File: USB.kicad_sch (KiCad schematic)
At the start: 41 parts, among them CON1 MicroSD_socket, J4 24FLZ-SM2-TB, Q1 AO3401A, U3 FDS9926A

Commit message: All key features are in the schematic.
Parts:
- added J3: PDM MEMS Mic, symbol Connector_Generic:Conn_01x05
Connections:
- net +3.3V: now also J3.1 (Pin_1)
- net GND: now also J3.2 (Pin_2), J3.3 (Pin_3)
- new net DMIC_CLK: J3.4 (Pin_4)
- new net DMIC_DATA: J3.5 (Pin_5)

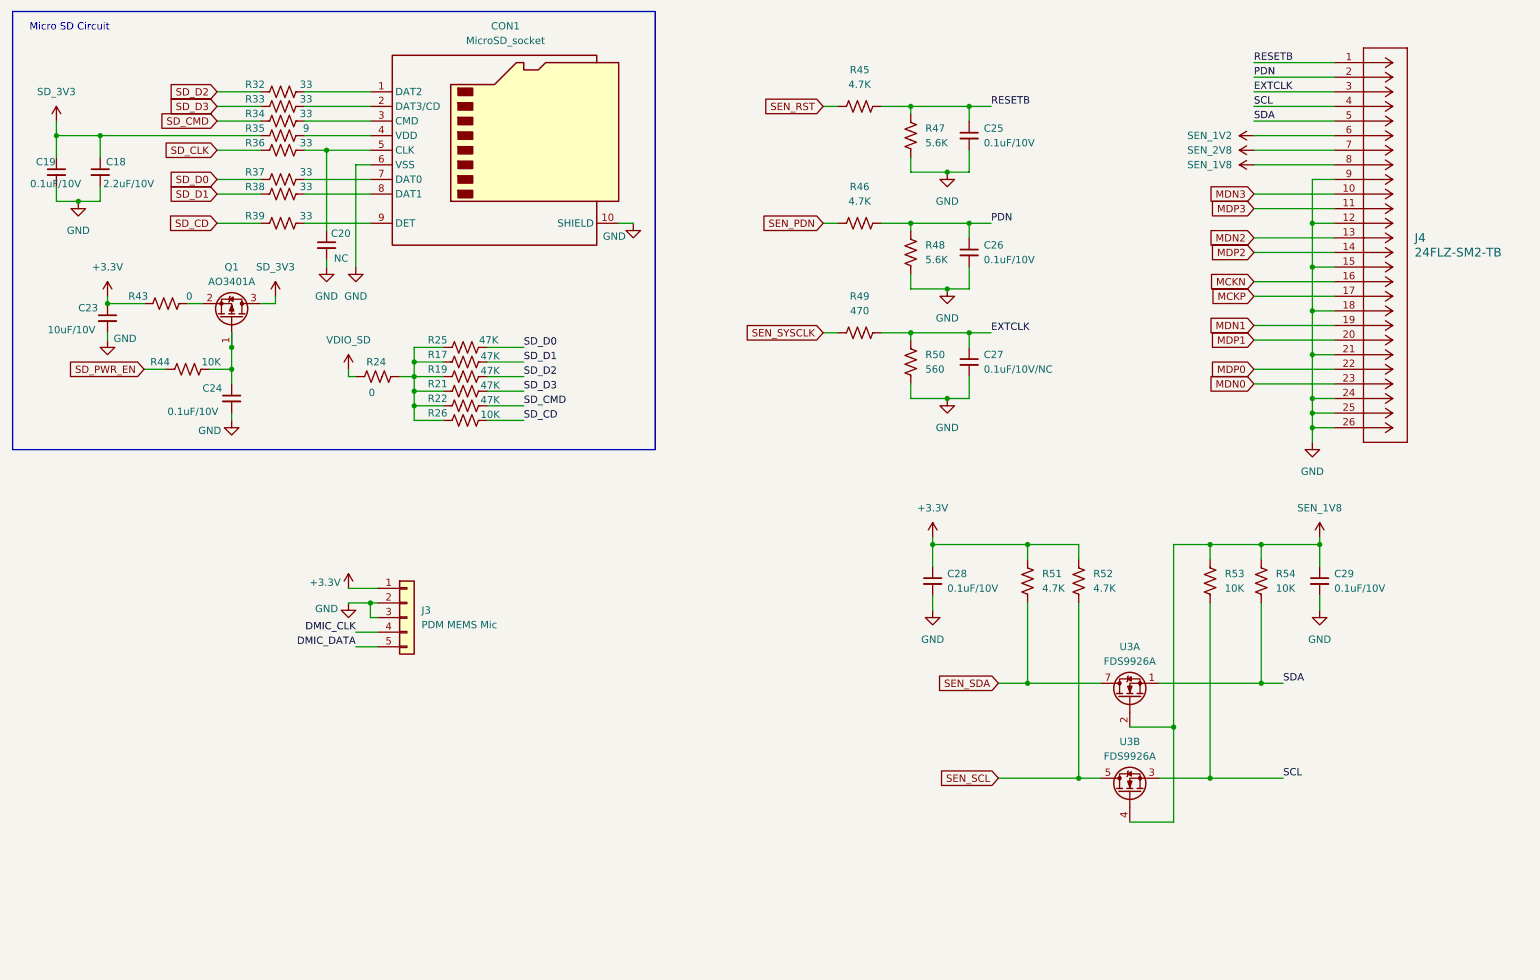
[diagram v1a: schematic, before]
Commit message: All footprints configured correctly. Next step is layout
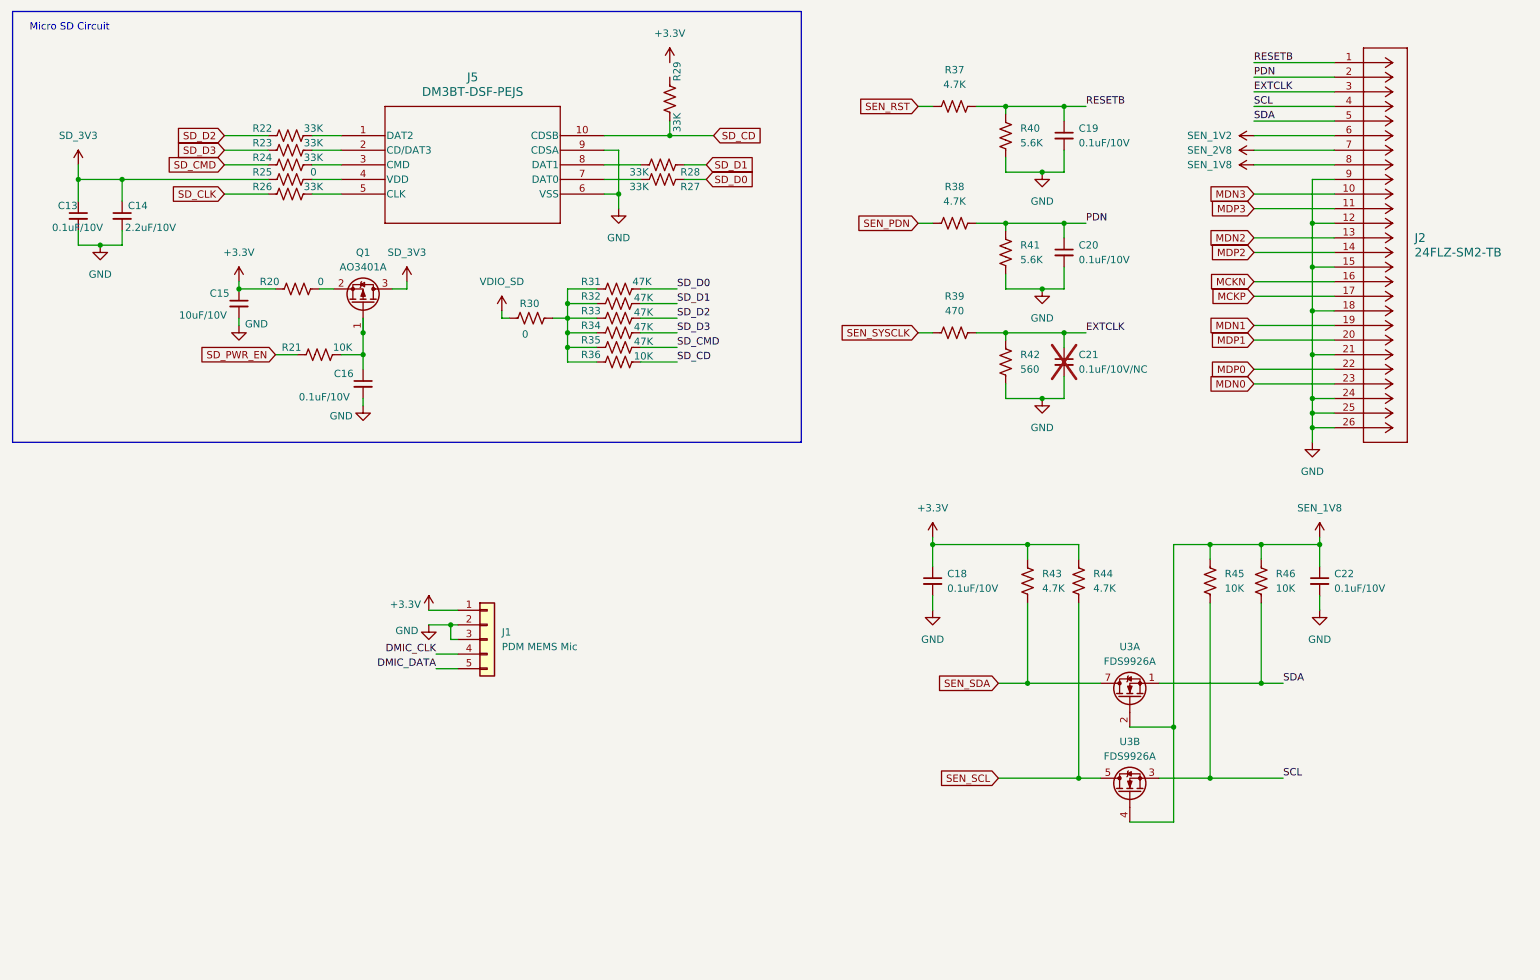
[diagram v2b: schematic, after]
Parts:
- removed C20: NC, symbol Device:C_Small
- removed CON1: MicroSD_socket, symbol Connector:Micro_SD_Card_Det1
- added J5: DM3BT-DSF-PEJS, DM3BT-DSF-PEJS_HIR, symbol 2026-01-21_09-53-59:DM3BT-DSF-PEJS
- C13: renamed from C19; footprint (none) -> Capacitor_SMD:C_0201_0603Metric_Pad0.64x0.40mm_HandSolder
- C14: renamed from C18; footprint (none) -> Capacitor_SMD:C_0201_0603Metric_Pad0.64x0.40mm_HandSolder
- C15: renamed from C23; footprint (none) -> Capacitor_SMD:C_0201_0603Metric_Pad0.64x0.40mm_HandSolder
- C16: renamed from C24; footprint (none) -> Capacitor_SMD:C_0201_0603Metric_Pad0.64x0.40mm_HandSolder
- C18: renamed from C28; footprint (none) -> Capacitor_SMD:C_0201_0603Metric_Pad0.64x0.40mm_HandSolder
- C19: renamed from C25; footprint (none) -> Capacitor_SMD:C_0201_0603Metric_Pad0.64x0.40mm_HandSolder
- C20: renamed from C26; footprint (none) -> Capacitor_SMD:C_0201_0603Metric_Pad0.64x0.40mm_HandSolder
- C21: renamed from C27; footprint (none) -> Capacitor_SMD:C_0201_0603Metric_Pad0.64x0.40mm_HandSolder; now not fitted
- C22: renamed from C29; footprint (none) -> Capacitor_SMD:C_0201_0603Metric_Pad0.64x0.40mm_HandSolder
- J1: renamed from J3; footprint (none) -> Adafruit:Adafruit MEMS 3492
- R20: renamed from R43; footprint (none) -> Resistor_SMD:R_0201_0603Metric_Pad0.64x0.40mm_HandSolder
- R21: renamed from R44; footprint (none) -> Resistor_SMD:R_0201_0603Metric_Pad0.64x0.40mm_HandSolder
- R22: renamed from R32; value 33 -> 33K; footprint (none) -> Resistor_SMD:R_0201_0603Metric_Pad0.64x0.40mm_HandSolder
- R23: renamed from R33; value 33 -> 33K; footprint (none) -> Resistor_SMD:R_0201_0603Metric_Pad0.64x0.40mm_HandSolder
- R24: renamed from R34; value 33 -> 33K; footprint (none) -> Resistor_SMD:R_0201_0603Metric_Pad0.64x0.40mm_HandSolder
- R25: renamed from R35; value 9 -> 0; footprint (none) -> Resistor_SMD:R_0201_0603Metric_Pad0.64x0.40mm_HandSolder
- R26: renamed from R36; value 33 -> 33K; footprint (none) -> Resistor_SMD:R_0201_0603Metric_Pad0.64x0.40mm_HandSolder
- R27: renamed from R37; value 33 -> 33K; footprint (none) -> Resistor_SMD:R_0201_0603Metric_Pad0.64x0.40mm_HandSolder
- R28: renamed from R38; value 33 -> 33K; footprint (none) -> Resistor_SMD:R_0201_0603Metric_Pad0.64x0.40mm_HandSolder
- R29: renamed from R39; value 33 -> 33K; footprint (none) -> Resistor_SMD:R_0201_0603Metric_Pad0.64x0.40mm_HandSolder
- R30: renamed from R24; footprint (none) -> Resistor_SMD:R_0201_0603Metric_Pad0.64x0.40mm_HandSolder
- R31: renamed from R25; footprint (none) -> Resistor_SMD:R_0201_0603Metric_Pad0.64x0.40mm_HandSolder
- R32: renamed from R17; footprint (none) -> Resistor_SMD:R_0201_0603Metric_Pad0.64x0.40mm_HandSolder
- R33: renamed from R19; footprint (none) -> Resistor_SMD:R_0201_0603Metric_Pad0.64x0.40mm_HandSolder
- R34: renamed from R21; footprint (none) -> Resistor_SMD:R_0201_0603Metric_Pad0.64x0.40mm_HandSolder
- R35: renamed from R22; footprint (none) -> Resistor_SMD:R_0201_0603Metric_Pad0.64x0.40mm_HandSolder
- R36: renamed from R26; footprint (none) -> Resistor_SMD:R_0201_0603Metric_Pad0.64x0.40mm_HandSolder
- R37: renamed from R45; footprint (none) -> Resistor_SMD:R_0201_0603Metric_Pad0.64x0.40mm_HandSolder
- R38: renamed from R46; footprint (none) -> Resistor_SMD:R_0201_0603Metric_Pad0.64x0.40mm_HandSolder
- R39: renamed from R49; footprint (none) -> Resistor_SMD:R_0201_0603Metric_Pad0.64x0.40mm_HandSolder
- R40: renamed from R47; footprint (none) -> Resistor_SMD:R_0201_0603Metric_Pad0.64x0.40mm_HandSolder
- R41: renamed from R48; footprint (none) -> Resistor_SMD:R_0201_0603Metric_Pad0.64x0.40mm_HandSolder
- R42: renamed from R50; footprint (none) -> Resistor_SMD:R_0201_0603Metric_Pad0.64x0.40mm_HandSolder
- R43: renamed from R51; footprint (none) -> Resistor_SMD:R_0201_0603Metric_Pad0.64x0.40mm_HandSolder
- R44: renamed from R52; footprint (none) -> Resistor_SMD:R_0201_0603Metric_Pad0.64x0.40mm_HandSolder
- R45: renamed from R53; footprint (none) -> Resistor_SMD:R_0201_0603Metric_Pad0.64x0.40mm_HandSolder
- R46: renamed from R54; footprint (none) -> Resistor_SMD:R_0201_0603Metric_Pad0.64x0.40mm_HandSolder
- renumbered J4 to J2
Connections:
- net GND: now also J5.6 (VSS), J5.9 (CDSA)
- net SD_CD: now also R29.2, J5.10 (CDSB); no longer R29.1
- net at R24.2: now also J5.3 (CMD)
- net at R28.2: now also J5.8 (DAT1)
- net at R27.2: now also J5.7 (DAT0)
- net at R25.2: now also J5.4 (VDD)
- net at R26.2: now also J5.5 (CLK)
- net at R23.2: now also J5.2 (CD/DAT3)
- net at R22.2: now also J5.1 (DAT2)
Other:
- moved on the sheet: C13, C14, C15, C16, C19, C20, J1, Q1, R20, R21, R22, R23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

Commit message: In the middle of layout. WIP
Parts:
- removed R20, R25, R30: 0, Resistor_SMD:R_0201_0603Metric_Pad0.64x0.40mm_HandSolder, symbol Device:R_US
- added TP6: SD_3.3V_TP, TestPoint:TestPoint_Pad_D1.5mm, symbol Connector:TestPoint
- C13, C16, C18, C19, C20, C22: value 0.1uF/10V -> 0.1uF
- C14: value 2.2uF/10V -> 2.2uF
- C15: value 10uF/10V -> 10uF
- C21: value 0.1uF/10V/NC -> 0.1uF/NC
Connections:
- net +3.3V: now also Q1.2 (S), R29.1
- net SD_3V3: now also J5.4 (VDD), TP6.1
- net VDIO_SD: now also R31.1, R32.1, R33.1, R34.1, R35.1, R36.1
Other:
- moved on the sheet: C15

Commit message: Breakthrough in PCB layout. WIP
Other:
- moved on the sheet: J1
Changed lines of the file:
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@@
 	)
 	(junction
-		(at 93.98 124.46)
+		(at 120.65 120.65)
 		(diameter 0)
 		(color 0 0 0 0)
@@
 	(wire
 		(pts
-			(xy 90.17 121.92) (xy 95.25 121.92)
+			(xy 116.84 118.11) (xy 121.92 118.11)
 		)
 		(stroke
@@
 	(wire
 		(pts
-			(xy 90.17 124.46) (xy 93.98 124.46)
+			(xy 116.84 120.65) (xy 120.65 120.65)
 		)
 		(stroke
@@
 	(wire
 		(pts
-			(xy 91.44 129.54) (xy 95.25 129.54)
+			(xy 118.11 125.73) (xy 121.92 125.73)
 		)
 		(stroke
@@
 	(wire
 		(pts
-			(xy 93.98 124.46) (xy 95.25 124.46)
+			(xy 120.65 120.65) (xy 121.92 120.65)
 		)
 		(stroke
@@
 	(wire
 		(pts
-			(xy 91.44 132.08) (xy 95.25 132.08)
+			(xy 118.11 128.27) (xy 121.92 128.27)
 		)
 		(stroke
@@
 	(wire
 		(pts
-			(xy 93.98 127) (xy 93.98 124.46)
+			(xy 120.65 123.19) (xy 120.65 120.65)
 		)
 		(stroke
@@
 	(wire
 		(pts
-			(xy 95.25 127) (xy 93.98 127)
+			(xy 121.92 123.19) (xy 120.65 123.19)
 		)
 		(stroke
@@
 		)
 	)
-	(label "SD_D2"
-		(at 133.35 71.12 0)
+	(label "SD_3V3"
+		(at 86.36 66.04 0)
+		(fields_autoplaced yes)
 		(effects
 			(font
@@
 			(justify left bottom)
 		)
+		(property "Netclass" "Power"
+			(at 86.36 67.31 0)
+			(effects
+				(font
+					(size 1.27 1.27)
+					(italic yes)
+				)
+				(justify left)
+			)
+		)
 	)
-	(label "DMIC_CLK"
-		(at 91.44 129.54 180)
+	(label "SD_D2"
+		(at 133.35 71.12 0)
 		(effects
 			(font
 				(size 1.27 1.27)
 			)
-			(justify right bottom)
+			(justify left bottom)
 		)
 	)
@@
 		)
 	)
-	(label "DMIC_DATA"
-		(at 91.44 132.08 180)
-		(effects
-			(font
-				(size 1.27 1.27)
-			)
-			(justify right bottom)
-		)
-	)
 	(label "RESETB"
 		(at 204.47 34.29 0)
@@
 		)
 	)
+	(global_label "DMIC_DATA"
+		(shape input)
+		(at 118.11 128.27 180)
+		(fields_autoplaced yes)
+		(effects
+			(font
+				(size 1.27 1.27)
+			)
+			(justify right)
+		)
+		(property "Intersheetrefs" "${INTERSHEET_REFS}"
+			(at 105.1462 128.27 0)
+			(effects
+				(font
+					(size 1.27 1.27)
+				)
+				(justify right)
+				(hide yes)
+			)
+		)
+	)
 	(global_label "MDP1"
 		(shape input)
@@
 		)
 	)
+	(global_label "DMIC_CLK"
+		(shape input)
+		(at 118.11 125.73 180)
+		(fields_autoplaced yes)
+		(effects
+			(font
+				(size 1.27 1.27)
+			)
+			(justify right)
+		)
+		(property "Intersheetrefs" "${INTERSHEET_REFS}"
+			(at 105.9929 125.73 0)
+			(effects
+				(font
+					(size 1.27 1.27)
+				)
+				(justify right)
+				(hide yes)
+			)
+		)
+	)
 	(global_label "SD_CMD"
 		(shape input)
@@
 	(symbol
 		(lib_id "power:GND")
-		(at 90.17 124.46 0)
+		(at 116.84 120.65 0)
 		(unit 1)
 		(exclude_from_sim no)
@@
 		(dnp no)
 		(property "Reference" "#PWR041"
-			(at 90.17 130.81 0)
+			(at 116.84 127 0)
 			(effects
 				(font
@@
 		)
 		(property "Value" "GND"
-			(at 86.36 125.476 0)
+			(at 113.03 121.666 0)
 			(effects
 				(font
@@
 		)
 		(property "Footprint" ""
-			(at 90.17 124.46 0)
+			(at 116.84 120.65 0)
 			(effects
 				(font
@@
 		)
 		(property "Datasheet" ""
-			(at 90.17 124.46 0)
+			(at 116.84 120.65 0)
 			(effects
 				(font
@@
 		)
 		(property "Description" "Power symbol creates a global label with name \"GND\" , ground"
-			(at 90.17 124.46 0)
+			(at 116.84 120.65 0)
 			(effects
 				(font
@@
 	(symbol
 		(lib_id "Connector_Generic:Conn_01x05")
-		(at 100.33 127 0)
+		(at 127 123.19 0)
 		(unit 1)
 		(exclude_from_sim no)
@@
 		(fields_autoplaced yes)
 		(property "Reference" "J1"
-			(at 102.87 125.7299 0)
+			(at 129.54 121.9199 0)
 			(effects
 				(font
@@
 		)
 		(property "Value" "PDM MEMS Mic"
-			(at 102.87 128.2699 0)
+			(at 129.54 124.4599 0)
 			(effects
 				(font
@@
 		)
 		(property "Footprint" "Adafruit:Adafruit MEMS 3492"
-			(at 100.33 127 0)
+			(at 127 123.19 0)
 			(effects
 				(font
@@
 		)
 		(property "Datasheet" "~"
-			(at 100.33 127 0)
+			(at 127 123.19 0)
 			(effects
 				(font
@@
 		)
 		(property "Description" "Generic connector, single row, 01x05, script generated (kicad-library-utils/schlib/autogen/connector/)"
-			(at 100.33 127 0)
+			(at 127 123.19 0)
 			(effects
 				(font
@@
 	(symbol
 		(lib_id "power:+3.3V")
-		(at 90.17 121.92 0)
+		(at 116.84 118.11 0)
 		(unit 1)
 		(exclude_from_sim no)
@@
 		(dnp no)
 		(property "Reference" "#PWR040"
-			(at 90.17 125.73 0)
+			(at 116.84 121.92 0)
 			(effects
 				(font
@@
 		)
 		(property "Value" "+3.3V"
-			(at 86.106 120.904 0)
+			(at 112.776 117.094 0)
 			(effects
 				(font
@@
 		)
 		(property "Footprint" ""
-			(at 90.17 121.92 0)
+			(at 116.84 118.11 0)
 			(effects
 				(font
@@
 		)
 		(property "Datasheet" ""
-			(at 90.17 121.92 0)
+			(at 116.84 118.11 0)
 			(effects
 				(font
@@
 		)
 		(property "Description" "Power symbol creates a global label with name \"+3.3V\""
-			(at 90.17 121.92 0)
+			(at 116.84 118.11 0)
 			(effects
 				(font

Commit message: I think I'm done. Fingers crossed.
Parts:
- removed J1: PDM MEMS Mic, Adafruit:Adafruit MEMS 3492, symbol Connector_Generic:Conn_01x05
- added C17, C35: 0.1uF, Capacitor_SMD:C_0201_0603Metric_Pad0.64x0.40mm_HandSolder, symbol Device:C_Small
- added C34, C54: 1uF, Capacitor_SMD:C_0201_0603Metric_Pad0.64x0.40mm_HandSolder, symbol Device:C_Small
- added M1, M2: IMP34DT05TR, IMP34DT05TR, symbol IMP34DT05TR:IMP34DT05TR
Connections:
- net +3.3V: now also C17.2, C34.1, C35.2, C54.2, M1.1 (VDD), M1.2 (LR), M2.1 (VDD)
- net DMIC_CLK: now also M1.3 (CLK), M2.3 (CLK)
- net DMIC_DATA: now also M1.4 (DOUT), M2.4 (DOUT)
- net GND: now also C17.1, C34.2, C35.1, C54.1, M1.5 (GND_1), M1.6 (GND_2), M1.7 (GND_3), M1.8 (GND_4), M2.2 (LR), M2.5 (GND_1), M2.6 (GND_2), M2.7 (GND_3), M2.8 (GND_4)
